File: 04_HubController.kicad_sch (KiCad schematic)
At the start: 0 parts

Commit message: add usb hub controller schematic, fix up redriver
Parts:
- added U13: CYUSB3304-68LTXx, symbol CakeUSB:CYUSB3304-68LTXx
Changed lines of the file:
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@@
 (kicad_sch (version 20230121) (generator eeschema)
   (paper "A4")
+  (symbol (lib_id "CakeUSB:CYUSB3304-68LTXx") (at 135.89 85.09 0) (unit 1)
+    (in_bom yes) (on_board yes) (dnp no)
+    (property "Reference" "U13" (at 165.1 39.37 0)
+      (effects (font (size 1.27 1.27)) (justify left))
+    )
+    (property "Value" "CYUSB3304-68LTXx" (at 165.1 130.81 0)
+      (effects (font (size 1.27 1.27)) (justify left))
+    )
+    (property "Footprint" "" (at 135.89 85.09 0)
+      (effects (font (size 1.27 1.27)) hide)
+    )
+    (property "Datasheet" "https://www.infineon.com/dgdl/Infineon-CYUSB330x_CYUSB331x_CYUSB332x_HX3_USB_3.0_Hub-DataSheet-v21_00-EN.pdf?fileId=8ac78c8c7d0d8da4017d0ecb53f644b8" (at 236.22 17.78 0)
+      (effects (font (size 1.27 1.27)) hide)
+    )
+    (pin "34")
+    (pin "30")
+    (pin "35")
+    (pin "44")
+    (pin "48")
+    (pin "11")
+    (pin "36")
+    (pin "37")
+    (pin "51")
+    (pin "24")
+    (pin "18")
+    (pin "31")
+    (pin "47")
+    (pin "32")
+    (pin "49")
+    (pin "50")
+    (pin "52")
+    (pin "22")
+    (pin "54")
+    (pin "28")
+    (pin "12")
+    (pin "40")
+    (pin "41")
+    (pin "13")
+    (pin "38")
+    (pin "43")
+    (pin "45")
+    (pin "46")
+    (pin "55")
+    (pin "56")
+    (pin "4")
+    (pin "58")
+    (pin "59")
+    (pin "16")
+    (pin "19")
+    (pin "60")
+    (pin "61")
+    (pin "63")
+    (pin "64")
+    (pin "5")
+    (pin "62")
+    (pin "42")
+    (pin "21")
+    (pin "14")
+    (pin "2")
+    (pin "26")
+    (pin "57")
+    (pin "6")
+    (pin "10")
+    (pin "65")
+    (pin "66")
+    (pin "67")
+    (pin "53")
+    (pin "39")
+    (pin "23")
+    (pin "15")
+    (pin "25")
+    (pin "27")
+    (pin "29")
+    (pin "3")
+    (pin "33")
+    (pin "1")
+    (pin "20")
+    (pin "17")
+    (pin "9")
+    (pin "68")
+    (pin "69")
+    (pin "7")
+    (pin "8")
+    (instances
+      (project "USBHUB"
+        (path "/d5edc647-9ac3-4ac1-ab8a-57c77be3f4d3/ab1e5fbe-3be5-47b1-a048-7835d2aad0d1"
+          (reference "U13") (unit 1)
+        )
+      )
+    )
+  )
 )

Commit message: WIP hub and DFP
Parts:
- added C100, C101, C102, C103, C104, C41, C42, C46, C48, C50, C65, C67, C69, C71, C73, C88, C91, C97, C98, C99: 100n, symbol Device:C_Small
- added C38, C39: 10p, symbol Device:C
- added C40, C43, C47, C49, C51, C54, C56, C58, C60, C62, C68, C70, C72, C74, C77, C79, C81, C83, C85, C90: 10n, symbol Device:C_Small
- added C44, C53, C64, C76, C87, C92: 1u, symbol Device:C_Small
- added C45, C52, C66, C75, C89: 22u, symbol Device:C_Small
- added C55, C57, C59, C61, C63, C78, C80, C82, C84, C86: 1n, symbol Device:C_Small
- added D11: LED, symbol Device:LED
- added FB1, FB2: BLM21PG221SN1D, symbol Device:FerriteBead_Small
- added J2: Conn_01x03_Pin, symbol Connector:Conn_01x03_Pin
- added R31, R32: 2k1, symbol Device:R
- added R33, R34, R38, R39: 10k, symbol Device:R
- added R35: R, symbol Device:R
- added R36: 6k04_1%, symbol Device:R
- added R37: 200_1%, symbol Device:R
- added Y1: 26MHz, symbol Device:Crystal_GND24
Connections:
- net DVDD12: now reaches U13.1 (DVDD12)
- net DVDD12: now also U13.19 (VDD_EFUSE), U13.27 (DVDD12), U13.3 (DVDD12), C67.1, C68.1, C69.1, C70.1, C71.1, C72.1, C73.1, C74.1, C75.1, C76.1, FB2.2
- net +1V2: now reaches U13.10 (AVDD12)
- net +1V2: now also U13.13 (DVDD12), U13.16 (AVDD12), U13.34 (AVDD12), U13.37 (DVDD12), U13.43 (DVDD12), U13.46 (AVDD12), U13.49 (DVDD12), U13.52 (AVDD12), U13.53 (AVDD12), U13.7 (DVDD12), C54.1, C55.1, C56.1, C57.1, C58.1, C59.1, C60.1, C61.1, C62.1, C63.1, C64.1, C65.1, C66.1, C77.1, C78.1, C79.1, C80.1, C81.1, C82.1, C83.1, C84.1, C85.1, C86.1, C87.1, C88.1, C89.1, C90.1, C91.1, C92.1, FB2.1
- net at U13.11 (DS4_TXP): now also C103.1
- net at U13.12 (DS4_TXM): now also C104.1
- net HUB1_DS4_RXM: now reaches U13.14 (DS4_RXM)
- net HUB1_DS4_RXP: now reaches U13.15 (DS4_RXP)
- net +5V: now reaches U13.17 (VBUS_US)
- net +5V: now also U13.18 (VBUS_DS)
- net at U13.2 (RREF_USB2): now also R36.1
- net SUSPEND: now reaches U13.20 (SUSPEND)
- net SUSPEND: now also D11.2 (A)
- net at U13.21 (RESERVED1): now also R33.1
- net at U13.22 (RESERVED2): now also R34.1
- net at U13.23 (MODE_SEL[0]): now also R39.2
- net at U13.24 (MODE_SEL[1]): now also R38.2
- net at U13.26 (RREF_SS): now also R37.2
- net +3V3: now reaches U13.28 (VDD_IO)
- net +3V3: now also U13.56 (AVDD33), U13.61 (AVDD33), U13.66 (AVDD33), C40.1, C41.1, C46.1, C47.1, C48.1, C49.1, C50.1, C51.1, C52.1, C53.1, FB1.1, R31.1, R32.1, R33.2, R34.2, R38.1
- net HUB1_PWR_EN: now reaches U13.29 (PWR_EN)
- net HUB1_OVRCURR: now reaches U13.30 (OVRCURR)
- net RESETN: now reaches U13.31 (RESETN)
- net I2C_CLK: now reaches U13.32 (I2C_CLK)
- net I2C_CLK: now also J2.1 (Pin_1), R32.2
- net I2C_DATA: now reaches U13.33 (I2C_DATA)
- net I2C_DATA: now also J2.2 (Pin_2), R31.2
- net HUB1_DS3_RXP: now reaches U13.35 (DS3_RXP)
- net HUB1_DS3_RXM: now reaches U13.36 (DS3_RXM)
- net at U13.38 (DS3_TXP): now also C101.1
- net at U13.39 (DS3_TXM): now also C102.1
- net at U13.4 (AVDD33): now also C42.1, C43.1, C44.1, C45.1, FB1.2
- net GND: now reaches U13.40 (GND)
- net GND: now also U13.69 (GND), C38.2, C39.2, C40.2, C41.2, C42.2, C43.2, C44.2, C45.2, C46.2, C47.2, C48.2, C49.2, C50.2, C51.2, C52.2, C53.2, C54.2, C55.2, C56.2, C57.2, C58.2, C59.2, C60.2, C61.2, C62.2, C63.2, C64.2, C65.2, C66.2, C67.2, C68.2, C69.2, C70.2, C71.2, C72.2, C73.2, C74.2, C75.2, C76.2, C77.2, C78.2, C79.2, C80.2, C81.2, C82.2, C83.2, C84.2, C85.2, C86.2, C87.2, C88.2, C89.2, C90.2, C91.2, C92.2, J2.3 (Pin_3), R35.2, R36.2, R37.1, R39.1, Y1.2, Y1.4
- net at U13.41 (DS2_TXP): now also C99.1
- net at U13.42 (DS2_TXM): now also C100.1
- net HUB1_DS2_RXM: now reaches U13.44 (DS2_RXM)
- net HUB1_DS2_RXP: now reaches U13.45 (DS2_RXP)
- net at U13.47 (DS1_TXP): now also C97.1
- net at U13.48 (DS1_TXM): now also C98.1
- net USB_UFP_TXN: now reaches U13.5 (US_TXM)
- net HUB1_DS1_RXM: now reaches U13.50 (DS1_RXM)
- net HUB1_DS1_RXP: now reaches U13.51 (DS1_RXP)
- net at U13.54 (XTL_OUT): now also C38.1, Y1.1
- net at U13.55 (XTL_IN): now also C39.1, Y1.3
- net USB_UFP_DP: now reaches U13.57 (US_DP)
- net USB_UFP_DM: now reaches U13.58 (US_DM)
- net HUB1_DS1_DM: now reaches U13.59 (DS1_DM)
- net USB_UFP_TXP: now reaches U13.6 (US_TXP)
- net HUB1_DS1_DP: now reaches U13.60 (DS1_DP)
- net HUB1_DS2_DP: now reaches U13.62 (DS2_DP)
- net HUB1_DS2_DM: now reaches U13.63 (DS2_DM)
- net HUB1_DS3_DM: now reaches U13.64 (DS3_DM)
- net HUB1_DS3_DP: now reaches U13.65 (DS3_DP)
- net HUB1_DS4_DP: now reaches U13.67 (DS4_DP)
- net HUB1_DS4_DM: now reaches U13.68 (DS4_DM)
- net USB_UFP_RXN: now reaches U13.8 (US_RXM)
- net USB_UFP_RXP: now reaches U13.9 (US_RXP)
- new net: D11.1 (K), R35.1
- new net HUB1_DS1_TXM: C98.2
- new net HUB1_DS1_TXP: C97.2
- new net HUB1_DS2_TXM: C100.2
- new net HUB1_DS2_TXP: C99.2
- new net HUB1_DS3_TXM: C102.2
- new net HUB1_DS3_TXP: C101.2
- new net HUB1_DS4_TXM: C104.2
- new net HUB1_DS4_TXP: C103.2
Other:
- note added: ""The VBUS_US pin should be connected to the VBUS from the US port. This signal is used to detect the US port connection to a Host or a hub.""
- note added: "Decoupling taken from HX3 Hardware Design Guidelines"
- note added: "Hub Controller"
- note added: "I2C"
- note added: "Implement RESETN logic here"
- note added: "Requires a crystal of 26MHz +- 150ppm, <200uW drive level Parallel resonant, fundamental mode Selected: TXM26M0004322CBCDO00T 100uW 9pF Approximating C_stray as 4pF; using eqn from page 5 of the HX3 Design guidelines C_1 = C_2 = 2 * (C_L - C_S) = 2 * (9 - 4) = 10pF"
- note added: "SUSPEND LED"
- note added: "The RESETN pin must be held LOW until both 3.3V and 1.2V supplies are stable."
- note added: "These precision resistors should be close to the IC and have a short ground path."
- note added: "This MODE_SEL is for configuration using an external I2C master"
- moved on the sheet: U13

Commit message: finish up schematics and ERC
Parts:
- added C120: 22u, symbol Device:C
- added R40: 10k, symbol Device:R
- renumbered C58 to C100, C59 to C101, C56 to C102, C57 to C103, C54 to C104, C55 to C105, C45 to C106, C44 to C107, C42 to C108, C43 to C109, C41 to C110, C40 to C111, C52 to C112, C53 to C113, C50 to C114, C51 to C115, C48 to C116, C49 to C117, C46 to C118, C47 to C119, C38 to C57, C39 to C58, C89 to C59, C87 to C60, C88 to C61, C97 to C62, C98 to C63, C92 to C64, C90 to C65, C91 to C66, C85 to C67, C86 to C68, C83 to C69, C84 to C70, C81 to C71, C82 to C72, C79 to C73, C80 to C74, C77 to C75, C78 to C76, C99 to C77, C100 to C78, C75 to C79, C76 to C80, C73 to C81, C74 to C82, C71 to C83, C72 to C84, C69 to C85, C70 to C86, C67 to C87, C68 to C88, C101 to C89, C102 to C90, C103 to C91, C104 to C92, C66 to C93, C64 to C94, C65 to C95, C62 to C96, C63 to C97, C60 to C98, C61 to C99, D11 to D27, FB2 to FB5, FB1 to FB6, R37 to R31, R36 to R32, R38 to R33, R39 to R35, R33 to R36, R31 to R37, R32 to R38, R35 to R39, U13 to U16
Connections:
- net +3V3: now also R40.1
- net GND: now also C120.2
- net RESETN: now also C120.1, R40.2
- net HUB1_PWR_EN renamed HUB1_PWR_EN_DS
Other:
- note added: "RC Delay for RESETN"
- note added: "~220ms reset timing, perhaps a little excessive"
- note removed: "Implement RESETN logic here"

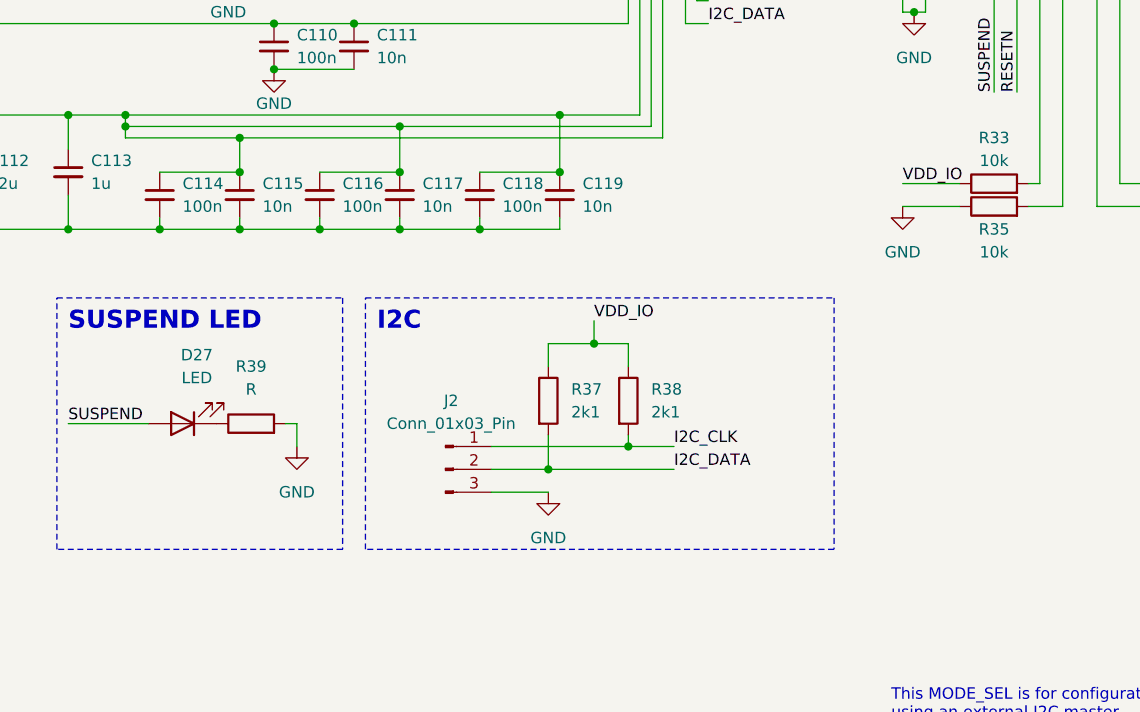
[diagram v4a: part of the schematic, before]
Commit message: finish setting footprints
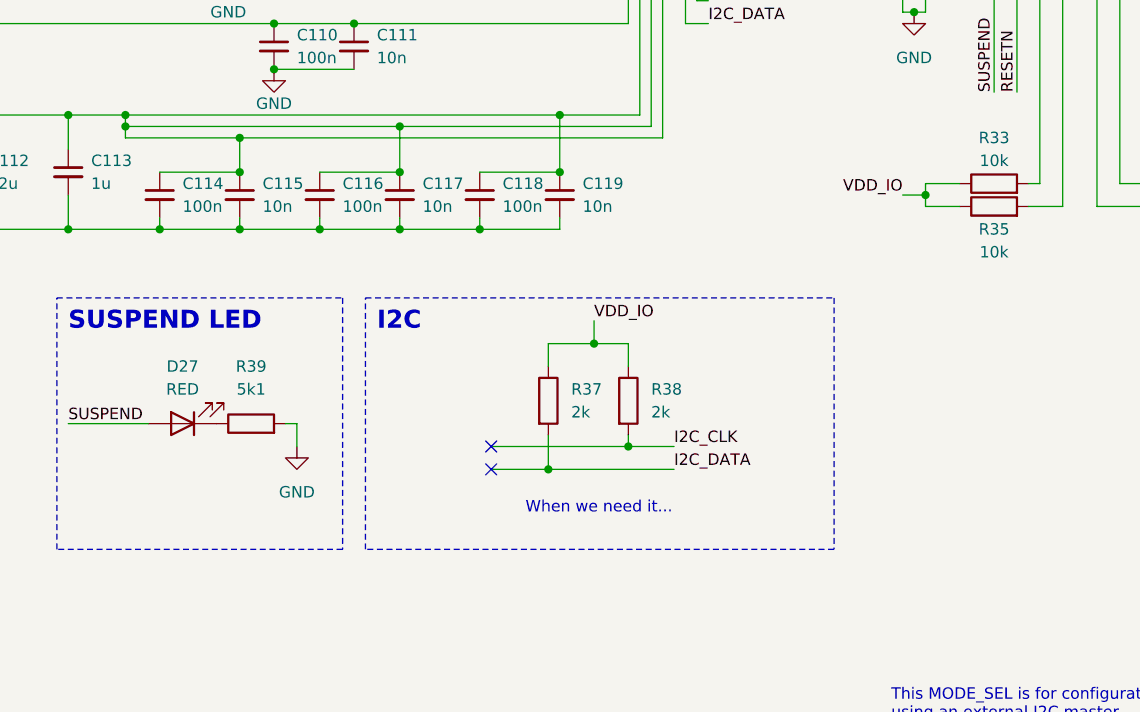
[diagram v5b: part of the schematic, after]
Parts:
- removed J2: Conn_01x03_Pin, symbol Connector:Conn_01x03_Pin
- C100, C101, C102, C103, C104, C105, C108, C109, C110, C111, C114, C115, C116, C117, C118, C119, C57, C58, C61, C62, C63, C65, C66, C67, C68, C69, C70, C71, C72, C73, C74, C75, C76, C77, C78, C81, C82, C83, C84, C85, C86, C87, C88, C89, C90, C91, C92, C95, C96, C97, C98, C99: footprint (none) -> Capacitor_SMD:C_0402_1005Metric
- C106, C107, C112, C113, C120, C59, C60, C64, C79, C80, C93, C94: footprint (none) -> Capacitor_SMD:C_0603_1608Metric
- D27: value LED -> RED; footprint (none) -> LED_SMD:LED_0603_1608Metric
- FB5, FB6: footprint (none) -> Inductor_SMD:L_0805_2012Metric
- R31, R32: footprint (none) -> Resistor_SMD:R_0402_1005Metric
- R33, R34, R35, R36, R40: footprint (none) -> Resistor_SMD:R_0603_1608Metric
- R37, R38: value 2k1 -> 2k; footprint (none) -> Resistor_SMD:R_0402_1005Metric
- R39: value R -> 5k1; footprint (none) -> Resistor_SMD:R_0603_1608Metric
- U16: footprint (none) -> CakeUSB:CYUSB3304-68LTXx
- Y1: footprint (none) -> Crystal:Crystal_SMD_3225-4Pin_3.2x2.5mm
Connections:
- net +3V3: now also R35.1
- net GND: no longer R35.1
- no-connect marks 0 -> 2
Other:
- note added: "When we need it..."

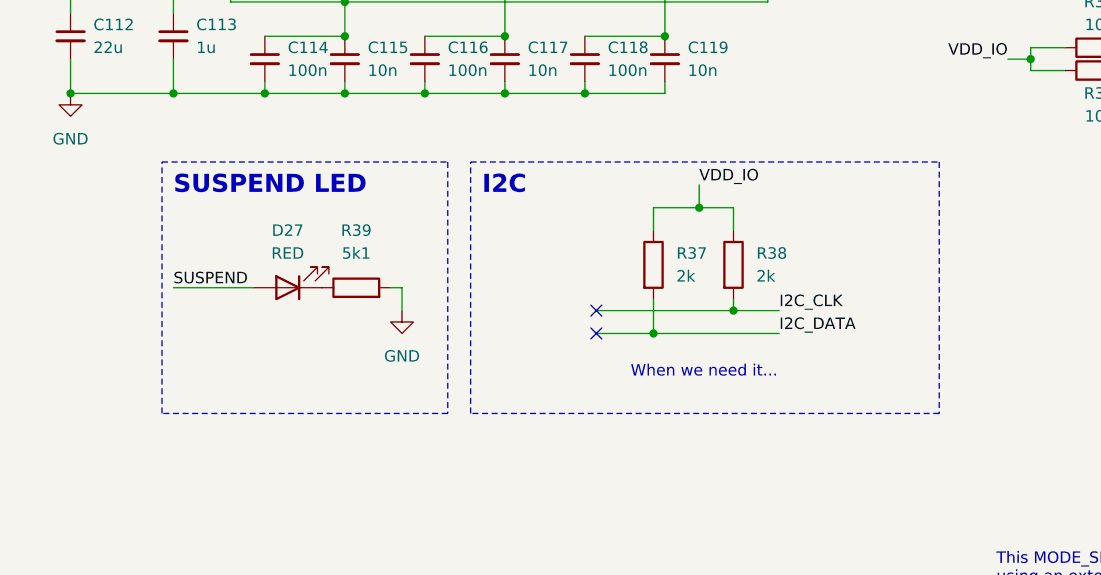
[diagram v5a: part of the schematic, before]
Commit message: symbol fixes, switch ESD protection for USB datalines
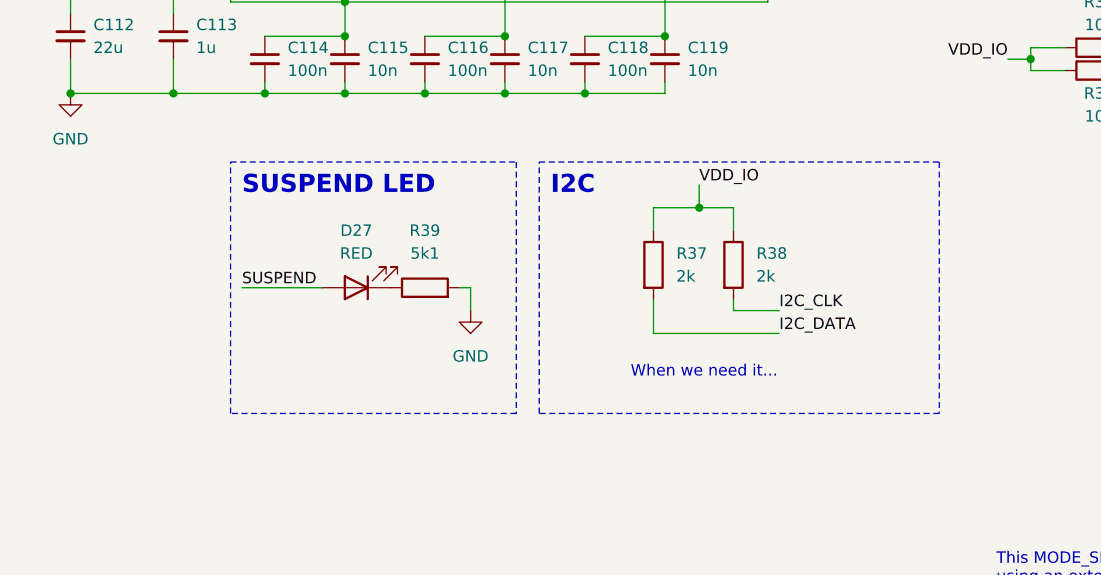
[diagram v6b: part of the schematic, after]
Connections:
- no-connect marks 2 -> 0
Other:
- moved on the sheet: D27, R39
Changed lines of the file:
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@@
   (junction (at 33.02 115.57) (diameter 0) (color 0 0 0 0)
   )
-  (junction (at 151.13 185.42) (diameter 0) (color 0 0 0 0)
-  )
   (junction (at 115.57 127) (diameter 0) (color 0 0 0 0)
   )
@@
   (junction (at 43.18 41.91) (diameter 0) (color 0 0 0 0)
   )
-  (junction (at 142.24 187.96) (diameter 0) (color 0 0 0 0)
-  )
   (junction (at 49.53 71.12) (diameter 0) (color 0 0 0 0)
   )
@@
   (junction (at 43.18 71.12) (diameter 0) (color 0 0 0 0)
   )
-  (no_connect (at 135.89 185.42))
-  (no_connect (at 135.89 187.96))
   (wire (pts (xy 78.74 64.77) (xy 86.36 64.77))
     (stroke (width 0) (type default))
@@
     (stroke (width 0) (type default))
   )
-  (wire (pts (xy 135.89 187.96) (xy 142.24 187.96))
-    (stroke (width 0) (type default))
-  )
   (wire (pts (xy 260.35 73.66) (xy 260.35 74.93))
     (stroke (width 0) (type default))
@@
     (stroke (width 0) (type default))
   )
-  (wire (pts (xy 113.03 182.88) (xy 114.3 182.88))
+  (wire (pts (xy 120.65 182.88) (xy 121.92 182.88))
     (stroke (width 0) (type default))
   )
@@
     (stroke (width 0) (type default))
   )
-  (wire (pts (xy 135.89 185.42) (xy 151.13 185.42))
-    (stroke (width 0) (type default))
-  )
   (wire (pts (xy 82.55 86.36) (xy 90.17 86.36))
     (stroke (width 0) (type default))
@@
     (stroke (width 0) (type default))
   )
-  (wire (pts (xy 114.3 182.88) (xy 114.3 185.42))
+  (wire (pts (xy 121.92 182.88) (xy 121.92 185.42))
     (stroke (width 0) (type default))
   )
@@
     (stroke (width 0) (type default))
   )
-  (wire (pts (xy 88.9 182.88) (xy 97.79 182.88))
+  (wire (pts (xy 96.52 182.88) (xy 105.41 182.88))
     (stroke (width 0) (type default))
   )
@@
     (stroke (width 0) (type default))
   )
-  (rectangle (start 87.63 168.91) (end 119.38 196.85)
+  (rectangle (start 95.25 168.91) (end 127 196.85)
     (stroke (width 0) (type dash))
     (fill (type none))
@@
     (fill (type none))
   )
-  (rectangle (start 121.92 168.91) (end 173.99 196.85)
+  (rectangle (start 129.54 168.91) (end 173.99 196.85)
     (stroke (width 0) (type dash))
     (fill (type none))
@@
     (effects (font (size 1.27 1.27)) (justify left bottom))
   )
-  (text "SUSPEND LED" (at 88.9 172.72 0)
+  (text "SUSPEND LED" (at 96.52 172.72 0)
     (effects (font (size 2 2) (thickness 0.4) bold) (justify left bottom))
   )
@@
     (effects (font (size 1.27 1.27)) (justify left bottom))
   )
-  (text "I2C" (at 123.19 172.72 0)
+  (text "I2C" (at 130.81 172.72 0)
     (effects (font (size 2 2) (thickness 0.4) bold) (justify left bottom))
   )
@@
     (effects (font (size 1.27 1.27)) (justify left bottom))
   )
-  (label "SUSPEND" (at 88.9 182.88 0) (fields_autoplaced)
+  (label "SUSPEND" (at 96.52 182.88 0) (fields_autoplaced)
     (effects (font (size 1.27 1.27)) (justify left bottom))
   )
@@
     )
   )
-  (symbol (lib_id "Device:R") (at 109.22 182.88 90) (unit 1)
-    (in_bom yes) (on_board yes) (dnp no) (fields_autoplaced)
-    (property "Reference" "R39" (at 109.22 176.53 90)
-      (effects (font (size 1.27 1.27)))
-    )
-    (property "Value" "5k1" (at 109.22 179.07 90)
-      (effects (font (size 1.27 1.27)))
-    )
-    (property "Footprint" "Resistor_SMD:R_0603_1608Metric" (at 109.22 184.658 90)
-      (effects (font (size 1.27 1.27)) hide)
-    )
-    (property "Datasheet" "~" (at 109.22 182.88 0)
+  (symbol (lib_id "Device:R") (at 116.84 182.88 90) (unit 1)
+    (in_bom yes) (on_board yes) (dnp no) (fields_autoplaced)
+    (property "Reference" "R39" (at 116.84 176.53 90)
+      (effects (font (size 1.27 1.27)))
+    )
+    (property "Value" "5k1" (at 116.84 179.07 90)
+      (effects (font (size 1.27 1.27)))
+    )
+    (property "Footprint" "Resistor_SMD:R_0603_1608Metric" (at 116.84 184.658 90)
+      (effects (font (size 1.27 1.27)) hide)
+    )
+    (property "Datasheet" "~" (at 116.84 182.88 0)
       (effects (font (size 1.27 1.27)) hide)
     )
@@
     )
   )
-  (symbol (lib_id "power:GND") (at 114.3 185.42 0) (unit 1)
-    (in_bom yes) (on_board yes) (dnp no) (fields_autoplaced)
-    (property "Reference" "#PWR094" (at 114.3 191.77 0)
-      (effects (font (size 1.27 1.27)) hide)
-    )
-    (property "Value" "GND" (at 114.3 190.5 0)
-      (effects (font (size 1.27 1.27)))
-    )
-    (property "Footprint" "" (at 114.3 185.42 0)
-      (effects (font (size 1.27 1.27)) hide)
-    )
-    (property "Datasheet" "" (at 114.3 185.42 0)
+  (symbol (lib_id "power:GND") (at 121.92 185.42 0) (unit 1)
+    (in_bom yes) (on_board yes) (dnp no) (fields_autoplaced)
+    (property "Reference" "#PWR094" (at 121.92 191.77 0)
+      (effects (font (size 1.27 1.27)) hide)
+    )
+    (property "Value" "GND" (at 121.92 190.5 0)
+      (effects (font (size 1.27 1.27)))
+    )
+    (property "Footprint" "" (at 121.92 185.42 0)
+      (effects (font (size 1.27 1.27)) hide)
+    )
+    (property "Datasheet" "" (at 121.92 185.42 0)
       (effects (font (size 1.27 1.27)) hide)
     )
@@
     )
   )
-  (symbol (lib_id "Device:LED") (at 101.6 182.88 180) (unit 1)
+  (symbol (lib_id "Device:LED") (at 109.22 182.88 180) (unit 1)
     (in_bom yes) (on_board yes) (dnp no)
-    (property "Reference" "D27" (at 101.6 176.53 0)
-      (effects (font (size 1.27 1.27)))
-    )
-    (property "Value" "RED" (at 101.6 179.07 0)
-      (effects (font (size 1.27 1.27)))
-    )
-    (property "Footprint" "LED_SMD:LED_0603_1608Metric" (at 101.6 182.88 0)
-      (effects (font (size 1.27 1.27)) hide)
-    )
-    (property "Datasheet" "~" (at 101.6 182.88 0)
-      (effects (font (size 1.27 1.27)) hide)
-    )
+    (property "Reference" "D27" (at 109.22 176.53 0)
+      (effects (font (size 1.27 1.27)))
+    )
+    (property "Value" "RED" (at 109.22 179.07 0)
+      (effects (font (size 1.27 1.27)))
+    )
+    (property "Footprint" "LED_SMD:LED_0603_1608Metric" (at 109.22 182.88 0)
+      (effects (font (size 1.27 1.27)) hide)
+    )
+    (property "Datasheet" "~" (at 109.22 182.88 0)
+      (effects (font (size 1.27 1.27)) hide)
+    )

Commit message: fix symbols, route UFP DPs and voltage regs
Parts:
- R33, R34, R35, R36, R40: footprint Resistor_SMD:R_0603_1608Metric -> Resistor_SMD:R_0402_1005Metric
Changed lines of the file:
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@@
       (effects (font (size 1.27 1.27)))
     )
-    (property "Footprint" "Resistor_SMD:R_0603_1608Metric" (at 191.77 157.988 90)
+    (property "Footprint" "Resistor_SMD:R_0402_1005Metric" (at 191.77 157.988 90)
       (effects (font (size 1.27 1.27)) hide)
     )
@@
       (effects (font (size 1.27 1.27)) (justify left))
     )
-    (property "Footprint" "Resistor_SMD:R_0603_1608Metric" (at 213.36 160.528 90)
+    (property "Footprint" "Resistor_SMD:R_0402_1005Metric" (at 213.36 160.528 90)
       (effects (font (size 1.27 1.27)) hide)
     )
@@
       (effects (font (size 1.27 1.27)))
     )
-    (property "Footprint" "Resistor_SMD:R_0603_1608Metric" (at 191.77 160.528 90)
+    (property "Footprint" "Resistor_SMD:R_0402_1005Metric" (at 191.77 160.528 90)
       (effects (font (size 1.27 1.27)) hide)
     )
@@
       (effects (font (size 1.27 1.27)))
     )
-    (property "Footprint" "Resistor_SMD:R_0603_1608Metric" (at 27.94 179.578 90)
+    (property "Footprint" "Resistor_SMD:R_0402_1005Metric" (at 27.94 179.578 90)
       (effects (font (size 1.27 1.27)) hide)
     )
@@
       (effects (font (size 1.27 1.27)) (justify left))
     )
-    (property "Footprint" "Resistor_SMD:R_0603_1608Metric" (at 213.36 157.988 90)
-      (effects (font (size 1.27 1.27)) hide)
-    )
+    (property "Footprint" "Resistor_SMD:R_0402_1005Metric" (at 213.36 157.988 90)
+      (effects (font (size 1.27 1.27)) hide)
+    )
